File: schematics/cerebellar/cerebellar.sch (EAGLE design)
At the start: 69 parts, among them CON2 ODrive1, CON4 Odrive3, CON5 ODrive4, CON6 Odrive2, CON7 ODrive5, CON8 ODrive6, IC2 SN75C3232, IC3 LTC7001, P1 Foot1, P10 SPI2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

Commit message: no message
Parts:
- removed C18, C2, C3, C4: 100nF, rcl:C-EU025-025X050
- removed C7: 1nF, rcl:C-EU025-025X050
- removed IC2: SN75C3232, MAX3232:MAX3232
- removed R11: 100k, rcl:R-EU_0204/7
- added P14: IMU, jst-ph:JST-PH5
- added R8: 1K, rcl:R-EU_0204/7
- P15: value Switch -> ON
- P4: value IMU -> LED; device jst-ph:JST-PH6 -> jst-ph:JST-PH2
- R1: value 10K -> 6.8k
- U$4: value MCP1725-ADJE/SN -> MAX769L; device MCP1725-ADJE_SN:MCP1725-ADJE/SN -> MAX869:MAX769L
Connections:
- removed net IMU-D+: P4.3
- removed net IMU_D-: P4.4
- removed net IMU_RX: IC2.T1OUT, P4.1
- removed net IMU_TX: IC2.R1IN, P4.2
- removed net N$11: C2.1, IC2.C2+
- removed net N$12: C2.2, IC2.C2-
- removed net N$13: C4.1, IC2.V+
- removed net N$14: C3.1, IC2.V-
- removed net N$25: R1.1, R11.2, U$4.ADJ
- removed net N$7: U$1.9-OUT1C, U$4.!SHDN
- removed net N$8: C18.2, IC2.C1-
- removed net VOUT_IMU: IC2.VCC, P4.5, R11.1, U$4.VOUT
- new net N$2: R1.1, U$4.SET
- net +5V: now also P14.4, U$4.IN; no longer U$4.VIN
- net GND: now also P14.5, P4.2; no longer C3.2, C4.2, C7.2, IC2.GND, P4.6
- net IMU_VDD: now also P14.1; no longer U$4.PWRGD
- net LED_PWM: now also U$4.ON/OFF
- net N$3: now also P4.1, R8.2; no longer C7.1, U$4.CDELAY
- net N$6: now also R8.1, U$4.OUT; no longer C18.1, IC2.C1+
- net T_RX: now also P14.3; no longer IC2.R1OUT
- net T_TX: now also P14.2; no longer IC2.T1IN
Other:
- note added: "Current and voltage measurement"
- note added: "Foot Sensor, analogue input"
- note added: "MOSFET Switch with Inrush control"
- note added: "PWM LED"
- note added: "Power supply 5V"
- note added: "uController"
- note removed: "Foot Sensor, coming in as analogue input"
- note removed: "Power supply 5V and 3.3V"
- moved on the sheet: C1, C10, C11, C12, C13, C16, C19, C9, CON2, CON4, CON5, CON6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

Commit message: added magnetssensor
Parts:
- removed R6: 100k, rcl:R-EU_0204/7
- added P17: MAG, jst-ph:JST-PH6
- LED1: value ON -> PWR
- LED3: value Mot ON -> Motor
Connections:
- net PWR_BATT- renamed BATT-
- removed net IMU_VDD: P14.1, R6.1, U$1.32-OUT1B
- removed net N$23: R6.2, U$1.3V3-3
- removed net PWR_BATT+: BATT1.+, BATT2.+, R3.1, SJ1.1
- new net IMU_ENABLE: P14.1, U$1.32-OUT1B
- new net MAG_EN: P17.2, U$1.9-OUT1C
- new net MAG_INT: P17.1, U$1.3-LRCLK2
- new net MAG_SCL: P17.3, U$1.16-A2/RX4/SCL1
- new net MAG_SDA: P17.4, U$1.17-A3/TX4/SDA1
- new net UC3.3V: P14.4, P17.5, U$1.3V3-3
- net +5V: no longer P14.4
- net BATT+: now also BATT1.+, BATT2.+, R3.1, SJ1.1
- net GND: now also P17.6
- net O4_RX: now also U$1.34-RX8; no longer U$1.16-A2/RX4/SCL1
- net O4_TX: now also U$1.35/TX8; no longer U$1.17-A3/TX4/SDA1

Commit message: added 3.3V power supply
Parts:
- added C2: 100nF, rcl:C-EU025-025X050
- added C4: 2.2uF, rcl:C-EU025-025X050
- added U$6: MAX884, MAX884:MAX884
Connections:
- removed net UC3.3V: P14.4, P17.5, U$1.3V3-3
- new net N$7: U$1.3V3-3
- net +3.3V: now also C4.1, P14.4, P17.5, U$6.OUT
- net +5V: now also C2.1, U$6.IN, U$6.LBI
- net BATT+: no longer C25.+, C26.1, R20.1, U$7.VS
- net GND: now also C2.2, C4.2, U$6.GND, U$6.SET
- net V+: now also C25.+, C26.1, R20.1, U$7.VS
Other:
- moved on the sheet: P1, P11, P12, P13, P14, P17, P2, P5, P6, P7, P8, P9

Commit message: doc
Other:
- note added: "PWM LED, 2A"
- note added: "Power supply 3.3V 200mA"
- note added: "Power supply 5V 500mA"
- note removed: "PWM LED"
- note removed: "Power supply 5V"
- moved on the sheet: P1, P11, P12, P13, P2, P5, P6, P7, P8, P9

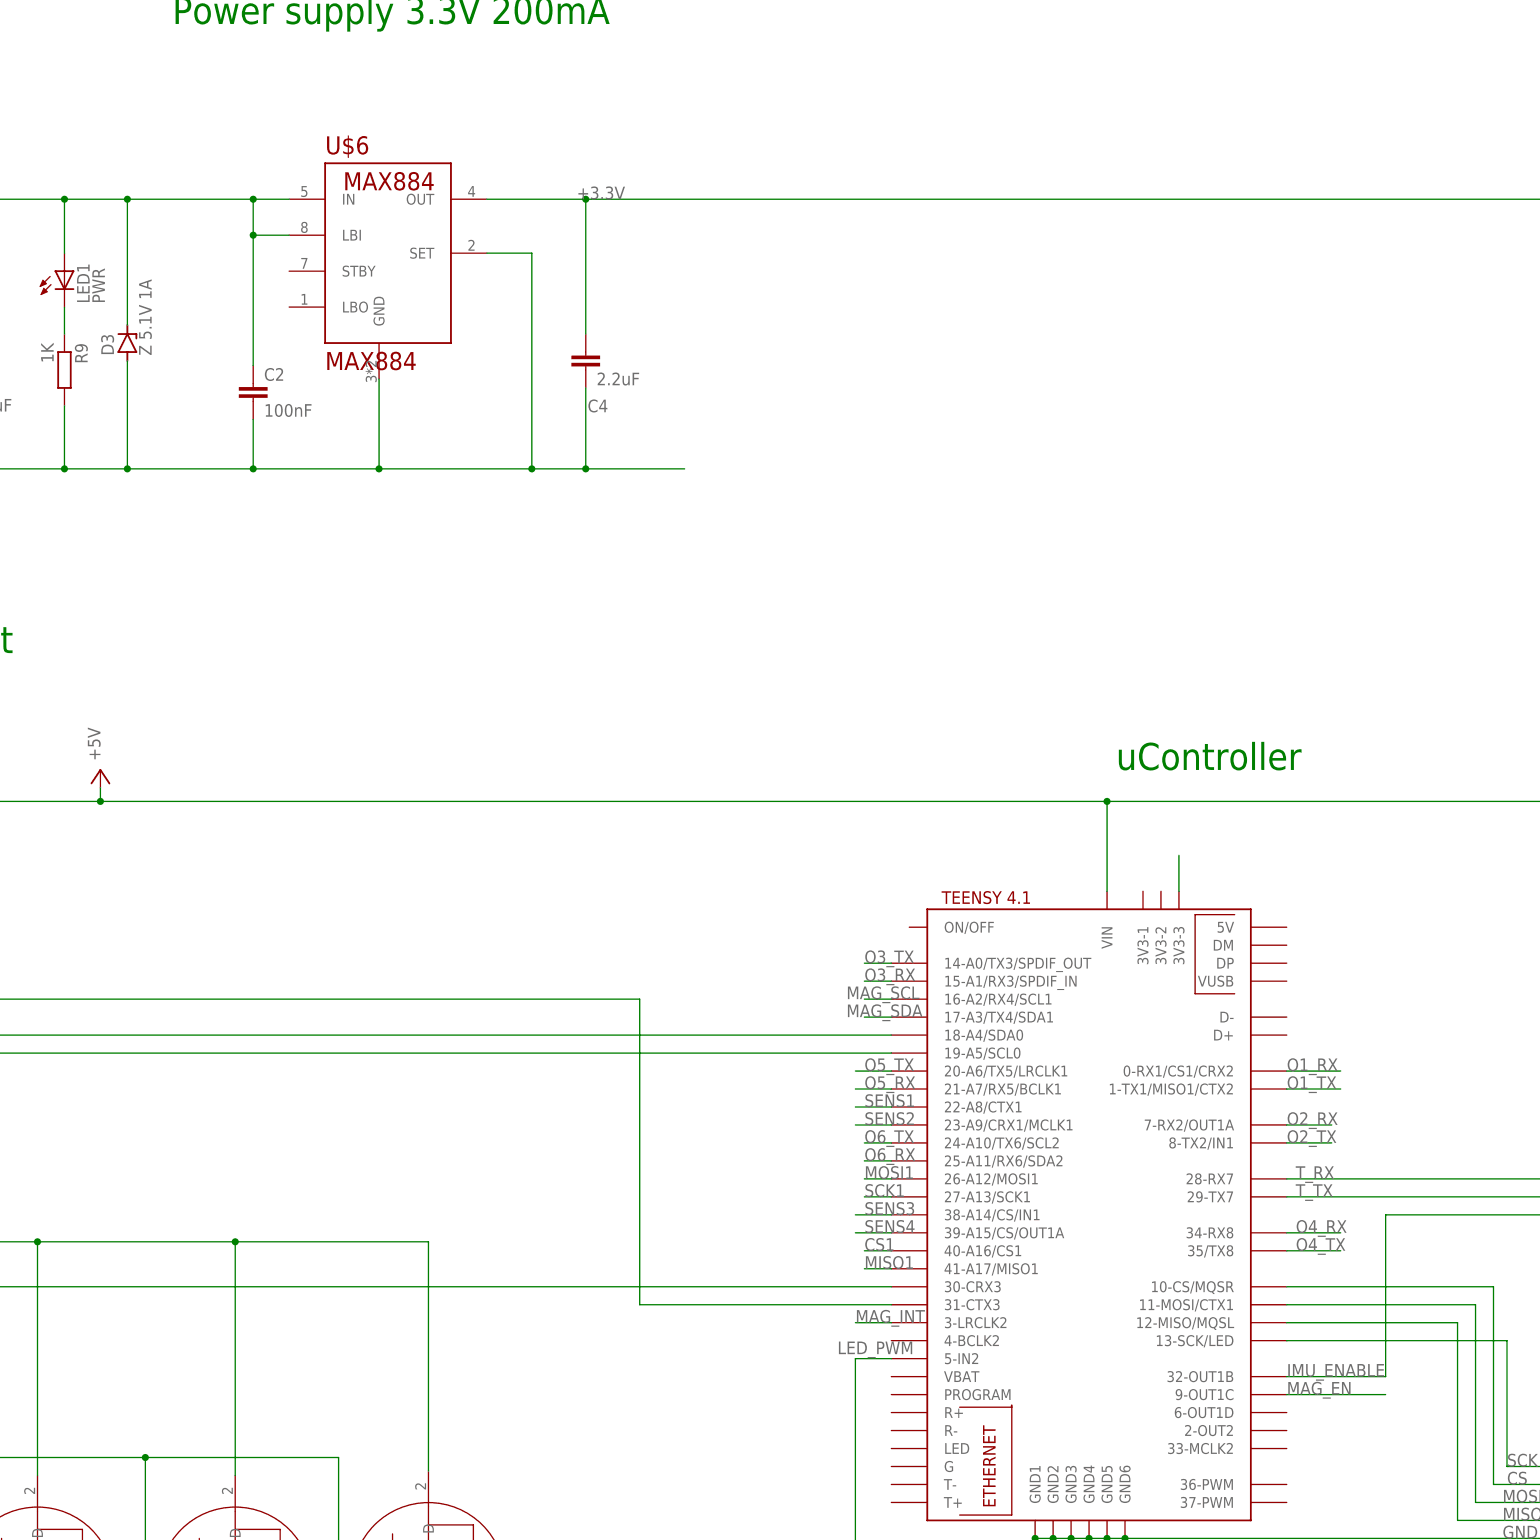
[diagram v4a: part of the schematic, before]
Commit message: Added Standby Line for 3.3. power supply
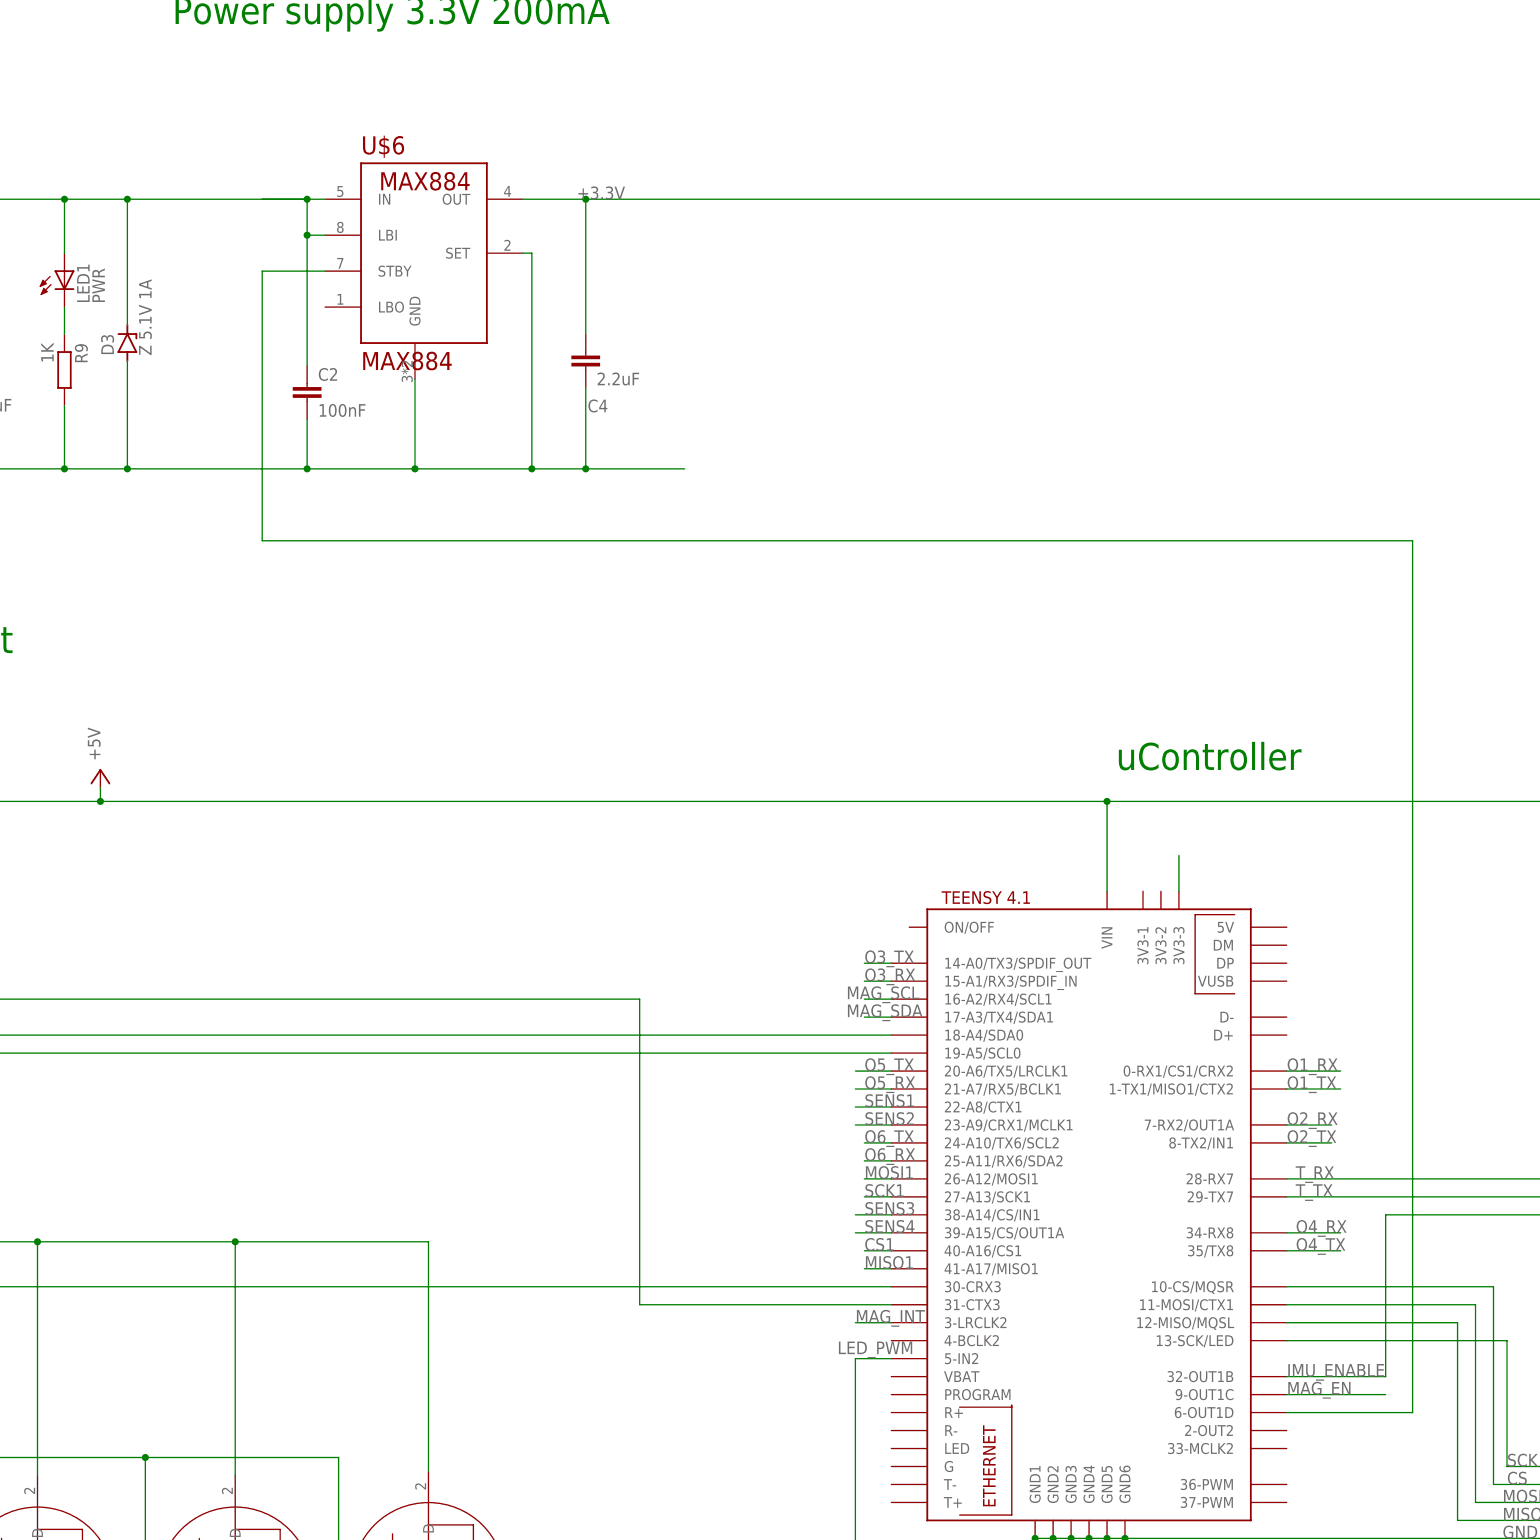
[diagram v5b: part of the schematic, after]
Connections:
- new net N$8: U$1.6-OUT1D, U$6.STBY
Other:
- moved on the sheet: C2, U$6
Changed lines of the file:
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@@
 <setting verticaltext="up"/>
 </settings>
-<grid distance="0.05" unitdist="inch" unit="inch" style="lines" multiple="1" display="no" altdistance="0.01" altunitdist="inch" altunit="inch"/>
+<grid distance="0.1" unitdist="inch" unit="inch" style="lines" multiple="1" display="no" altdistance="0.01" altunitdist="inch" altunit="inch"/>
 <layers>
 <layer number="1" name="Top" color="4" fill="1" visible="no" active="no"/>
@@
 <attribute name="VALUE" x="259.08" y="25.146" size="1.778" layer="96" rot="R180"/>
 </instance>
-<instance part="U$6" gate="G$1" x="21.59" y="167.64" smashed="yes">
-<attribute name="NAME" x="13.97" y="184.15" size="2.54" layer="94"/>
-<attribute name="VALUE" x="13.97" y="153.67" size="2.54" layer="94"/>
-</instance>
-<instance part="C2" gate="G$1" x="3.81" y="151.765" smashed="yes">
-<attribute name="NAME" x="5.334" y="152.146" size="1.778" layer="95"/>
-<attribute name="VALUE" x="5.334" y="147.066" size="1.778" layer="96"/>
+<instance part="U$6" gate="G$1" x="26.67" y="167.64" smashed="yes">
+<attribute name="NAME" x="19.05" y="184.15" size="2.54" layer="94"/>
+<attribute name="VALUE" x="19.05" y="153.67" size="2.54" layer="94"/>
+</instance>
+<instance part="C2" gate="G$1" x="11.43" y="151.765" smashed="yes">
+<attribute name="NAME" x="12.954" y="152.146" size="1.778" layer="95"/>
+<attribute name="VALUE" x="12.954" y="147.066" size="1.778" layer="96"/>
 </instance>
 <instance part="C4" gate="G$1" x="50.8" y="156.21" smashed="yes">
@@
 <wire x1="64.77" y1="139.7" x2="50.8" y2="139.7" width="0.1524" layer="91"/>
 <wire x1="50.8" y1="139.7" x2="43.18" y2="139.7" width="0.1524" layer="91"/>
-<wire x1="43.18" y1="139.7" x2="21.59" y2="139.7" width="0.1524" layer="91"/>
-<wire x1="21.59" y1="139.7" x2="3.81" y2="139.7" width="0.1524" layer="91"/>
-<wire x1="3.81" y1="139.7" x2="-13.97" y2="139.7" width="0.1524" layer="91"/>
+<wire x1="43.18" y1="139.7" x2="26.67" y2="139.7" width="0.1524" layer="91"/>
+<wire x1="26.67" y1="139.7" x2="11.43" y2="139.7" width="0.1524" layer="91"/>
+<wire x1="11.43" y1="139.7" x2="-13.97" y2="139.7" width="0.1524" layer="91"/>
 <wire x1="-13.97" y1="139.7" x2="-22.86" y2="139.7" width="0.1524" layer="91"/>
 <wire x1="-22.86" y1="148.59" x2="-22.86" y2="139.7" width="0.1524" layer="91"/>
@@
 <pinref part="D3" gate="G$1" pin="A"/>
 <pinref part="U$6" gate="G$1" pin="GND"/>
-<wire x1="21.59" y1="152.4" x2="21.59" y2="139.7" width="0.1524" layer="91"/>
-<junction x="21.59" y="139.7"/>
+<wire x1="26.67" y1="152.4" x2="26.67" y2="139.7" width="0.1524" layer="91"/>
+<junction x="26.67" y="139.7"/>
 <pinref part="C2" gate="G$1" pin="2"/>
-<wire x1="3.81" y1="146.685" x2="3.81" y2="139.7" width="0.1524" layer="91"/>
-<junction x="3.81" y="139.7"/>
+<wire x1="11.43" y1="146.685" x2="11.43" y2="139.7" width="0.1524" layer="91"/>
+<junction x="11.43" y="139.7"/>
 <pinref part="U$6" gate="G$1" pin="SET"/>
-<wire x1="36.83" y1="170.18" x2="43.18" y2="170.18" width="0.1524" layer="91"/>
+<wire x1="41.91" y1="170.18" x2="43.18" y2="170.18" width="0.1524" layer="91"/>
 <wire x1="43.18" y1="170.18" x2="43.18" y2="139.7" width="0.1524" layer="91"/>
 <junction x="43.18" y="139.7"/>
@@
 <pinref part="D3" gate="G$1" pin="C"/>
 <pinref part="U$6" gate="G$1" pin="IN"/>
-<wire x1="-13.97" y1="177.8" x2="3.81" y2="177.8" width="0.1524" layer="91"/>
+<wire x1="-13.97" y1="177.8" x2="11.43" y2="177.8" width="0.1524" layer="91"/>
 <pinref part="U$6" gate="G$1" pin="LBI"/>
-<wire x1="3.81" y1="177.8" x2="8.89" y2="177.8" width="0.1524" layer="91"/>
-<wire x1="8.89" y1="172.72" x2="3.81" y2="172.72" width="0.1524" layer="91"/>
-<wire x1="3.81" y1="172.72" x2="3.81" y2="177.8" width="0.1524" layer="91"/>
-<junction x="3.81" y="177.8"/>
+<wire x1="11.43" y1="177.8" x2="5.08" y2="177.8" width="0.1524" layer="91"/>
+<wire x1="11.43" y1="177.8" x2="13.97" y2="177.8" width="0.1524" layer="91"/>
+<wire x1="13.97" y1="172.72" x2="11.43" y2="172.72" width="0.1524" layer="91"/>
+<wire x1="11.43" y1="172.72" x2="11.43" y2="177.8" width="0.1524" layer="91"/>
+<junction x="11.43" y="177.8"/>
 <pinref part="C2" gate="G$1" pin="1"/>
-<wire x1="3.81" y1="172.72" x2="3.81" y2="154.305" width="0.1524" layer="91"/>
-<junction x="3.81" y="172.72"/>
+<wire x1="11.43" y1="172.72" x2="11.43" y2="154.305" width="0.1524" layer="91"/>
+<junction x="11.43" y="172.72"/>
 </segment>
 <segment>
@@
 <label x="224.79" y="49.53" size="1.778" layer="95"/>
 <pinref part="U$6" gate="G$1" pin="OUT"/>
-<wire x1="36.83" y1="177.8" x2="50.8" y2="177.8" width="0.1524" layer="91"/>
+<wire x1="41.91" y1="177.8" x2="50.8" y2="177.8" width="0.1524" layer="91"/>
 <label x="49.53" y="177.8" size="1.778" layer="95"/>
 <wire x1="50.8" y1="177.8" x2="50.8" y2="158.75" width="0.1524" layer="91"/>
@@
 </segment>
 </net>
+<net name="N$8" class="0">
+<segment>
+<pinref part="U$1" gate="G$1" pin="6-OUT1D"/>
+<wire x1="149.86" y1="6.35" x2="167.64" y2="6.35" width="0.1524" layer="91"/>
+<wire x1="167.64" y1="6.35" x2="167.64" y2="129.54" width="0.1524" layer="91"/>
+<wire x1="167.64" y1="129.54" x2="5.08" y2="129.54" width="0.1524" layer="91"/>
+<pinref part="U$6" gate="G$1" pin="STBY"/>
+<wire x1="5.08" y1="129.54" x2="5.08" y2="167.64" width="0.1524" layer="91"/>
+<wire x1="5.08" y1="167.64" x2="13.97" y2="167.64" width="0.1524" layer="91"/>
+</segment>
+</net>
